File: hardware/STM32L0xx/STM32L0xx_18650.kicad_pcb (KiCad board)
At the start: 2 copper layers, 109.7 x 16 mm, 50 parts, among them J2 Battery, J3 GPIO, J4 USB_B_Micro, J5 Power, J6 LEDs, J7 GPIO, Q1 BSS806N, Q2 BSS806N, Q3 BSS806N, Q4 BSS806N, SW1 Mode, SW2 Power, U1 STM32L072KZTx, U2 AP2210N-3.3TRG1, U3 MCP73833-AMI_UN, Y1 32.768kHz

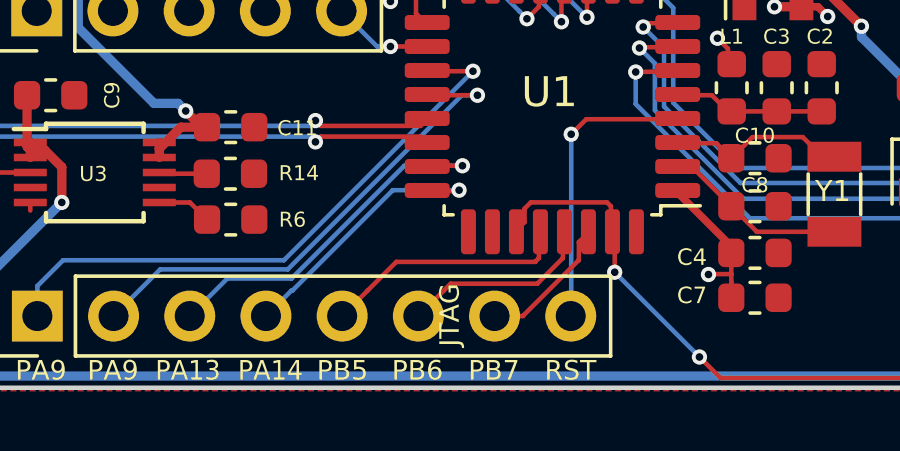
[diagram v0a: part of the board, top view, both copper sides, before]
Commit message: Create board pinout graphic
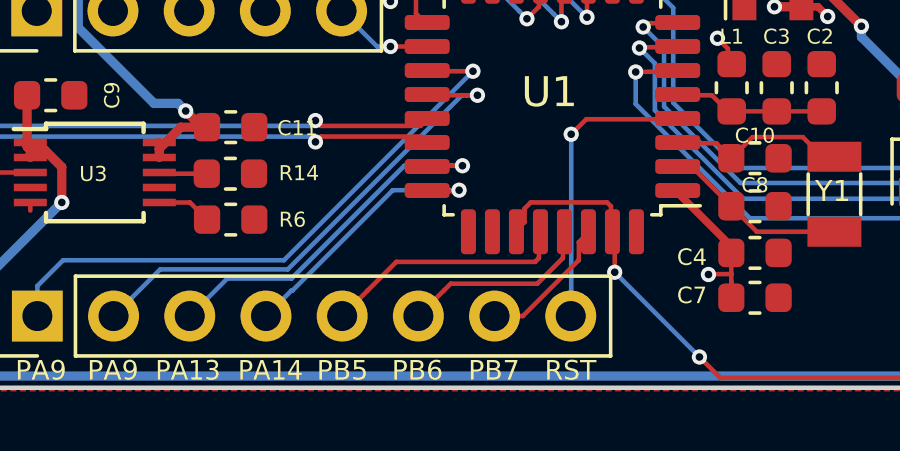
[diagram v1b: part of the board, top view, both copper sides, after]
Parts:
- J2: footprint Jeremy:Battery_Clips_18650 -> BatteryClips:Keystone54_18650_PTC
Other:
- board text removed: "JTAG"

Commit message: Hardware feedback.
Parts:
- removed REF**: OSHW-Logo2_7.3x6mm_Copper, Symbol:OSHW-Logo2_7.3x6mm_Copper
- added C12: 2.2uF, Capacitor_SMD:C_0603_1608Metric, F.Cu at (101.6, 93.8)
- added C13: 1.0uf, Capacitor_SMD:C_0603_1608Metric, F.Cu at (62.3, 106.9)
- added C6: 1.0uf, Capacitor_SMD:C_0603_1608Metric, F.Cu at (107.3, 98.0)
- added U4: TPD2E2U06, Package_TO_SOT_SMD:SOT-553, F.Cu at (88.8, 99.7)
- moved C11 0.08 mm to (86.0, 99.3)
- moved D1 0.08 mm to (61.8, 105.2)
- moved R6 0.08 mm to (86.0, 102.4)
- moved R14 0.07 mm to (86.0, 100.9)
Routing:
- net GND: track 7.70 -> 10.8 mm
- net /USB_D+: track 31.4 -> 34.5 mm
- net /VUSB: track 130.1 -> 131.5 mm
- net /VIN: track 51.4 -> 52.8 mm
- net /USB_D-: track 31.5 -> 32.7 mm
- net +3V3: track 17.5 -> 18.4 mm, vias 9 -> 10
- net /PA10: track 16.9 -> 17.6 mm

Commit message: Change USB TVS.
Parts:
- U4: value TPD2E2U06 -> ESD7002WTT1G; footprint Package_TO_SOT_SMD:SOT-553 -> Package_TO_SOT_SMD:SOT-323_SC-70
- moved U4 1.25 mm to (90.0, 99.4), turned to 180 degrees
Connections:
- U4 pad 1: (no net) -> /USB_D+
- U4 pad 2: (no net) -> /USB_D-
- U4 pad 3: /USB_D+ -> GND
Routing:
- net GND: track 10.8 -> 7.70 mm
- net /PA14: track 9.66 -> 11.7 mm
- net /USB_D+: track 34.5 -> 32.6 mm
- net /PA13: track 12.4 -> 13.3 mm
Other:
- board text added: "rev 1a4"
- board text removed: "rev 1a3"

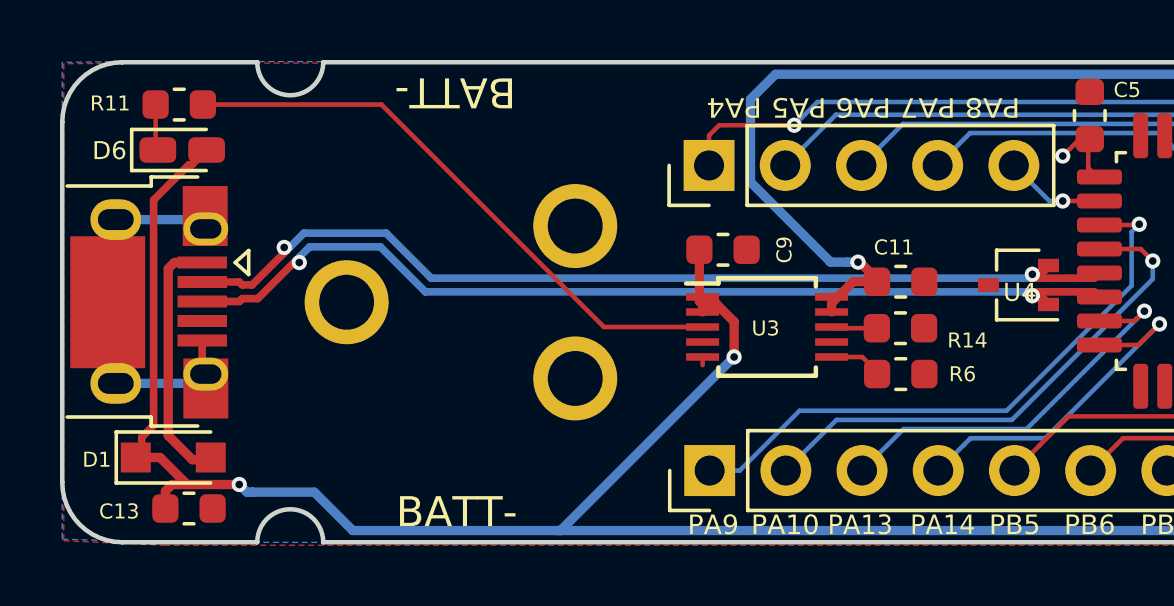
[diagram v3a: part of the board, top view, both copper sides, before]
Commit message: Change battery changing controller
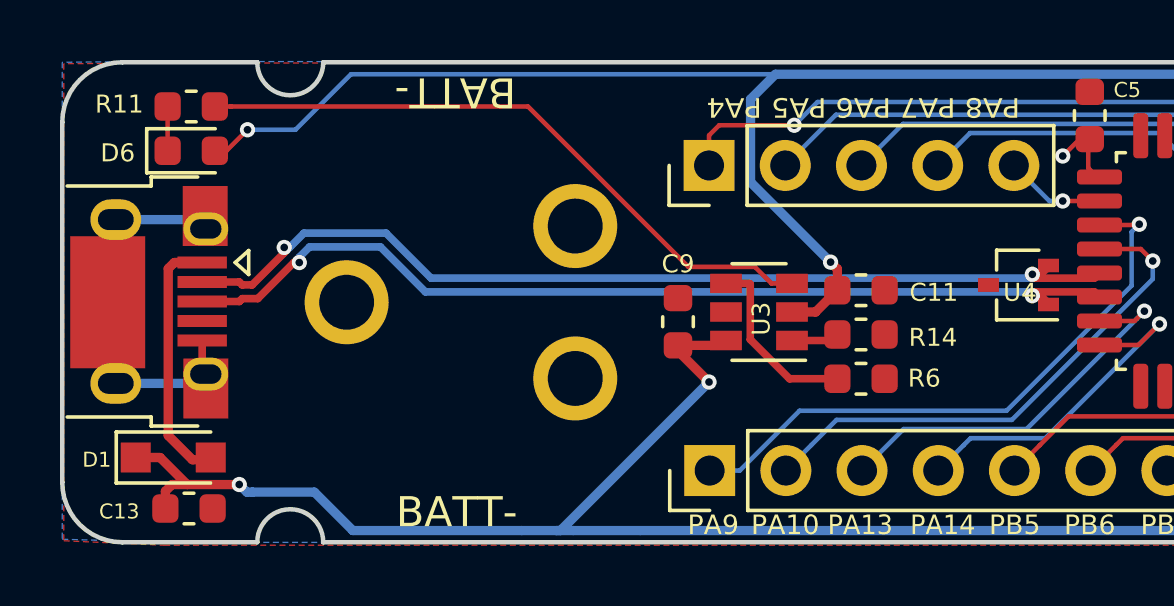
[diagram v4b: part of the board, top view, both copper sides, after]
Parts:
- D6: footprint LED_SMD:LED_0603_1608Metric_Castellated -> LED_SMD:LED_0603_1608Metric
- R6: value 1k -> 675
- U3: value MCP73833-AMI_UN -> BQ21040; footprint Package_SO:TSSOP-10_3x3mm_P0.5mm -> Package_TO_SOT_SMD:SOT-23-6
- moved C9 2.83 mm to (78.6, 100.7), turned to 90 degrees
- moved C11 1.36 mm to (84.7, 99.6)
- moved R6 1.33 mm to (84.7, 102.5)
- moved R14 1.33 mm to (84.7, 101.1)
- moved U3 0.57 mm to (81.3, 100.3), turned to 180 degrees
- moved R11 0.41 mm to (62.4, 93.5)
- moved D6 0.30 mm to (62.4, 95.0)
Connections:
- D6 pad 2: /VUSB -> +BATT
- U3 pad 1: /VUSB -> Net-(R14-Pad1)
- U3 pad 2: /VUSB -> +BATT
- U3 pad 4: (no net) -> Net-(R6-Pad1)
- U3 pad 6: Net-(R6-Pad1) -> /VUSB
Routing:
- net +BATT: track 69.7 -> 88.0 mm, vias 1 -> 2
- net /VUSB: track 131.5 -> 117.6 mm
- net Net-(R6-Pad1): track 1.83 -> 6.11 mm
- net Net-(R11-Pad1): track 19.7 -> 21.7 mm

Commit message: Add USART, I2C & SPI pins to silkscreen
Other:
- board text added: "(max 2.3A per)"
- board text added: "MISO"
- board text added: "MOSI"
- board text added: "RX"
- board text added: "SCL"
- board text added: "SCLK"
- board text added: "SDA"
- board text added: "TX"
- board text removed: "(max 2.3A per!)"
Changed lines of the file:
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@@
   (general
     (thickness 1.6)
-    (drawings 68)
+    (drawings 75)
     (tracks 392)
     (zones 0)
@@
   )
   (setup
-    (last_trace_width 0.31)
+    (last_trace_width 0.254)
     (user_trace_width 0.254)
     (user_trace_width 0.31)
@@
     (aux_axis_origin 0 0)
     (grid_origin 105.2 95.275)
-    (visible_elements FFFFFF7F)
+    (visible_elements FFFFFFFF)
     (pcbplotparams
       (layerselection 0x010fc_ffffffff)
@@
       (net 18 /PA8))
   )
+  (gr_text SCL (at 79.725 107.45) (layer B.SilkS)
+    (effects (font (size 0.65 0.65) (thickness 0.1)) (justify mirror))
+  )
+  (gr_text SDA (at 82.25 107.425) (layer B.SilkS)
+    (effects (font (size 0.65 0.6) (thickness 0.1)) (justify mirror))
+  )
+  (gr_text SCLK (at 82.2 93.6) (layer B.SilkS)
+    (effects (font (size 0.65 0.65) (thickness 0.1)) (justify mirror))
+  )
+  (gr_text MISO (at 84.8 93.6) (layer B.SilkS)
+    (effects (font (size 0.65 0.65) (thickness 0.1)) (justify mirror))
+  )
+  (gr_text MOSI (at 87.375 93.6) (layer B.SilkS)
+    (effects (font (size 0.65 0.65) (thickness 0.1)) (justify mirror))
+  )
+  (gr_text TX (at 92.4 107.425) (layer B.SilkS)
+    (effects (font (size 0.65 0.65) (thickness 0.1)) (justify mirror))
+  )
+  (gr_text RX (at 94.95 107.425) (layer B.SilkS)
+    (effects (font (size 0.65 0.65) (thickness 0.1)) (justify mirror))
+  )
   (gr_line (start 140 108) (end 155.65 108) (layer Edge.Cuts) (width 0.15))
   (gr_line (start 140.1 92) (end 155.65 92) (layer Edge.Cuts) (width 0.15))
@@
   )
   (gr_text "rev 1a4" (at 153.5 96.525) (layer B.SilkS)
-    (effects (font (size 0.75 0.75) (thickness 0.1)) (justify left mirror))
+    (effects (font (size 0.8 0.8) (thickness 0.1)) (justify left mirror))
   )
   (gr_text "GND USB+ 3.3v Batt+" (at 116.95 107.45) (layer F.SilkS)
@@
     (effects (font (size 0.65 0.65) (thickness 0.1)))
   )
-  (gr_text "Created by Jeremy Gillick" (at 146.825 105.375) (layer B.SilkS)
-    (effects (font (size 0.75 0.75) (thickness 0.1)) (justify mirror))
-  )
-  (gr_text "(max 2.3A per!)" (at 113.95 98.525) (layer B.SilkS)
-    (effects (font (size 0.65 0.65) (thickness 0.1)) (justify mirror))
+  (gr_text "Created by Jeremy Gillick" (at 153.9 105.375) (layer B.SilkS)
+    (effects (font (size 0.8 0.8) (thickness 0.1)) (justify left mirror))
+  )
+  (gr_text "(max 2.3A per)" (at 109.55 93.475) (layer B.SilkS)
+    (effects (font (size 0.7 0.7) (thickness 0.1)) (justify mirror))
   )
   (gr_line (start 157.85 92) (end 159.749999 91.999845) (layer Edge.Cuts) (width 0.15))
@@
     (effects (font (size 0.65 0.65) (thickness 0.1)) (justify mirror))
   )
-  (gr_text PA4 (at 79.65 97.4) (layer B.SilkS)
+  (gr_text PA4 (at 79.65 97.3) (layer B.SilkS)
     (effects (font (size 0.65 0.65) (thickness 0.1)) (justify mirror))
   )
@@
     (effects (font (size 0.65 0.65) (thickness 0.1)) (justify mirror))
   )
-  (gr_text PWM (at 113.95 93.475) (layer B.SilkS)
+  (gr_text PWM (at 115.65 93.525) (layer B.SilkS)
     (effects (font (size 1 1) (thickness 0.2)) (justify mirror))
   )
@@
   (segment (start 62.575 97.245) (end 62.885 97.555) (width 0.31) (layer B.Cu) (net 2) (status 30))
   (segment (start 59.885 97.245) (end 62.575 97.245) (width 0.31) (layer B.Cu) (net 2) (status 30))
-  (via (at 109.8 93.825) (size 0.508) (drill 0.254) (layers F.Cu B.Cu) (net 3))
-  (segment (start 109.5475 93.5725) (end 109.8 93.825) (width 0.1524) (layer F.Cu) (net 3))
-  (segment (start 109.5475 92.94) (end 109.5475 93.5725) (width 0.1524) (layer F.Cu) (net 3) (status 10))
   (via (at 113.85 93.85) (size 0.508) (drill 0.254) (layers F.Cu B.Cu) (net 3))
   (segment (start 112.9475 92.9475) (end 113.85 93.85) (width 0.1524) (layer F.Cu) (net 3) (status 10))
@@
   (via (at 104.25 94.725) (size 0.508) (drill 0.254) (layers F.Cu B.Cu) (net 3))
   (segment (start 104.25 95.3) (end 104.25 94.725) (width 0.31) (layer F.Cu) (net 3))
+  (segment (start 109.5475 93.5725) (end 109.8 93.825) (width 0.1524) (layer F.Cu) (net 3))
+  (segment (start 109.5475 92.94) (end 109.5475 93.5725) (width 0.1524) (layer F.Cu) (net 3) (status 10))
+  (via (at 109.8 93.825) (size 0.508) (drill 0.254) (layers F.Cu B.Cu) (net 3))
   (segment (start 123.33 105.61) (end 126.4 102.54) (width 0.762) (layer F.Cu) (net 4) (status 20))
   (segment (start 120.31 105.61) (end 123.33 105.61) (width 0.762) (layer F.Cu) (net 4) (status 10))

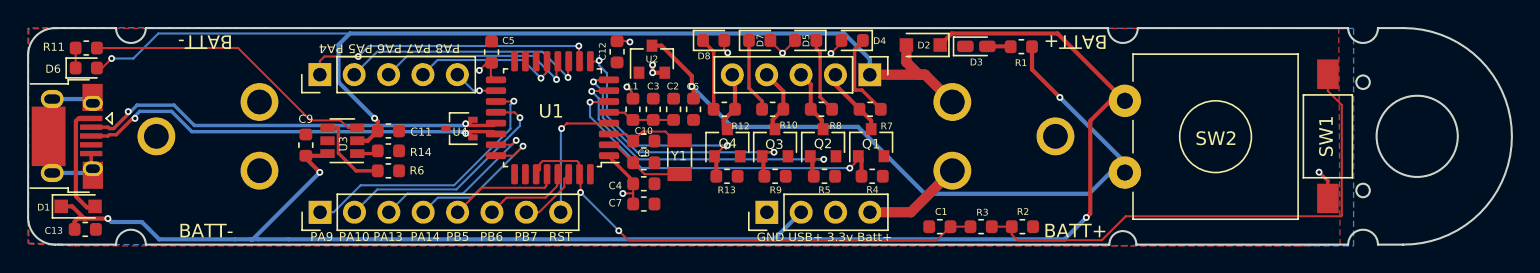
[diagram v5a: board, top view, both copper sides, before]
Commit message: Change BATT+ to Vin
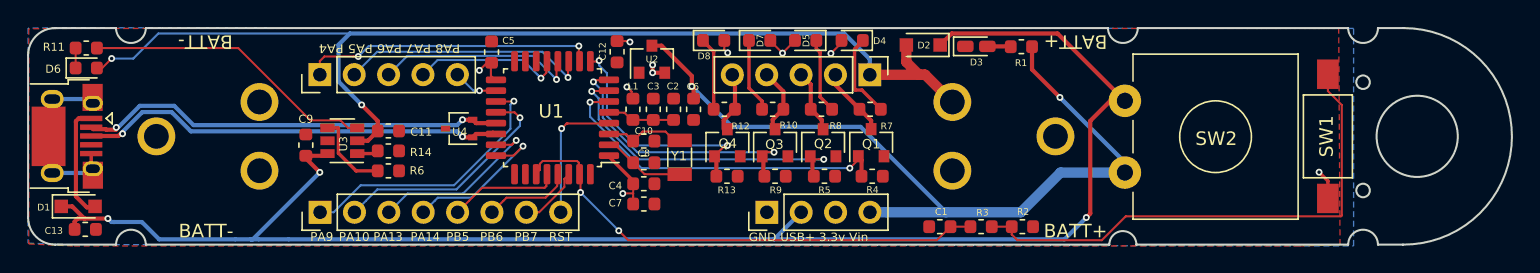
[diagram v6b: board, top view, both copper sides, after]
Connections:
- J5 pad 4: +BATT -> /VIN
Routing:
- net /VIN: track 52.6 -> 60.4 mm
- net +BATT: track 88.0 -> 80.6 mm
- net /USB_D+: track 32.6 -> 31.9 mm
- net /USB_D-: track 32.3 -> 31.7 mm
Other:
- board text added: "CLK"
- board text added: "DIO"
- board text added: "GND USB+ 3.3v Vin"
- board text added: "rev 1a5"
- board text removed: "GND USB+ 3.3v Batt+"
- board text removed: "rev 1a4"

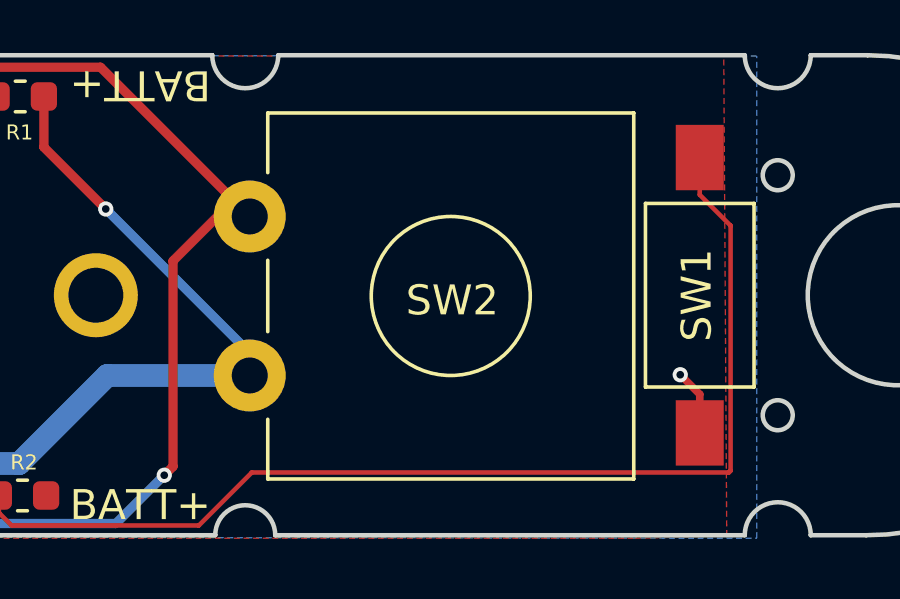
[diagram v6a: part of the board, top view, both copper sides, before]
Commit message: Add OSH logo
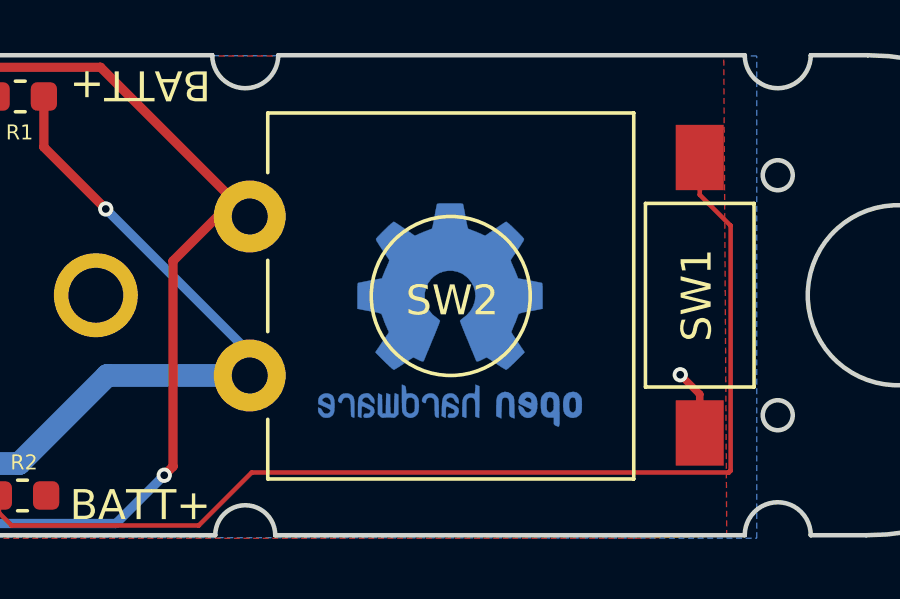
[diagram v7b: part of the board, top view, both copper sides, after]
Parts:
- added REF**: OSHW-Logo2_9.8x8mm_Copper, Symbol:OSHW-Logo2_9.8x8mm_Copper, B.Cu at (145.8, 100.7)

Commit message: Update text
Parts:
- moved REF** 0.46 mm to (145.9, 100.2)
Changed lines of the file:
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@@
   )
   (module Symbol:OSHW-Logo2_9.8x8mm_Copper (layer B.Cu)
-    (at 145.825 100.65 180)
+    (at 145.925 100.2 180)
     (descr "Open Source Hardware Symbol")
     (tags "Logo Symbol OSHW")
@@
       (effects (font (size 0.7 0.7) (thickness 0.1)))
     )
-    (fp_text user "With built-in protection circuit!" (at 0.05 1.225) (layer B.SilkS)
+    (fp_text user "With built-in protection circuit" (at 0.05 1.225) (layer B.SilkS)
       (effects (font (size 0.7 0.65) (thickness 0.08)) (justify mirror))
     )
